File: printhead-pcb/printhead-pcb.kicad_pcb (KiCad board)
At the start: 2 copper layers, 35 x 35 mm, 4 parts, among them U3 EMC2302-2-AIZL-TR, U4 EMC2302-2-AIZL-TR, U5 ADS1015IDGS, U6 PCA9536D

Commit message: circuit finished?
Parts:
- removed U5: ADS1015IDGS, Package_SO:TSSOP-10_3x3mm_P0.5mm
- removed U6: PCA9536D, Package_SO:SOIC-8_3.9x4.9mm_P1.27mm
- added C10: 0.22µF, Capacitor_SMD:C_0402_1005Metric, F.Cu at (154.0, 74.5)
- added C11: 0.1µF, Capacitor_SMD:C_0402_1005Metric, F.Cu at (151.0, 81.5)
- added C4: 0.1µF, Capacitor_SMD:C_0402_1005Metric, F.Cu at (139.5, 55.5)
- added C5: 0.1µF, Capacitor_SMD:C_0402_1005Metric, F.Cu at (136.1, 60.5)
- added C6: 0.1µF, Capacitor_SMD:C_0402_1005Metric, F.Cu at (132.0, 62.0)
- added C7: 0.1µFC, Capacitor_SMD:C_0402_1005Metric, F.Cu at (141.5, 62.0)
- added C8: 0.1µF, Capacitor_SMD:C_0402_1005Metric, F.Cu at (136.1, 66.4)
- added C9: 1µF, Capacitor_SMD:C_0402_1005Metric, F.Cu at (149.8, 75.1)
- added D1: GREEN, LED_SMD:LED_0805_2012Metric, F.Cu at (154.5, 79.5)
- added D2: YELLOW, LED_SMD:LED_0805_2012Metric, F.Cu at (158.9, 66.5)
- added D3: BLUE, LED_SMD:LED_0805_2012Metric, F.Cu at (131.5, 77.5)
- added D4: YELLOW, LED_SMD:LED_0805_2012Metric, F.Cu at (155.5, 71.0)
- added J1: FAN0, Connector_JST:JST_GH_SM02B-GHS-TB_1x02-1MP_P1.25mm_Horizontal, F.Cu at (133.0, 52.0)
- added J2: FAN2, Connector_JST:JST_GH_SM02B-GHS-TB_1x02-1MP_P1.25mm_Horizontal, F.Cu at (110.5, 52.0)
- added J3: FAN1, Connector_JST:JST_GH_SM02B-GHS-TB_1x02-1MP_P1.25mm_Horizontal, F.Cu at (110.2, 66.4)
- added J4: FAN3, Connector_JST:JST_GH_SM02B-GHS-TB_1x02-1MP_P1.25mm_Horizontal, F.Cu at (110.2, 73.9)
- added J5: T0, Connector_JST:JST_GH_SM02B-GHS-TB_1x02-1MP_P1.25mm_Horizontal, F.Cu at (125.5, 52.0)
- added J6: T1, Connector_JST:JST_GH_SM02B-GHS-TB_1x02-1MP_P1.25mm_Horizontal, F.Cu at (110.2, 59.0)
- added J7: T2, Connector_JST:JST_GH_SM02B-GHS-TB_1x02-1MP_P1.25mm_Horizontal, F.Cu at (110.2, 81.5)
- added J8: T3, Connector_JST:JST_GH_SM02B-GHS-TB_1x02-1MP_P1.25mm_Horizontal, F.Cu at (118.0, 52.0)
- added L2: L, Inductor_SMD:L_0402_1005Metric, F.Cu at (134.5, 71.0)
- added L3: L, Inductor_SMD:L_0402_1005Metric, F.Cu at (129.5, 69.0)
- added L4: L, Inductor_SMD:L_0402_1005Metric, F.Cu at (131.0, 73.0)
- added L5: L, Inductor_SMD:L_0402_1005Metric, F.Cu at (139.0, 66.5)
- added L6: L, Inductor_SMD:L_0402_1005Metric, F.Cu at (146.9, 75.1)
- added Q1: DTC143E, Package_TO_SOT_SMD:SOT-723, F.Cu at (122.1, 60.4)
- added Q2: DTC143E, Package_TO_SOT_SMD:SOT-723, F.Cu at (125.0, 61.5)
- added Q3: DTC143E, Package_TO_SOT_SMD:SOT-723, F.Cu at (128.9, 60.0)
- added Q4: DTC143E, Package_TO_SOT_SMD:SOT-723, F.Cu at (120.9, 71.0)
- added R1: 10k, Resistor_SMD:R_0402_1005Metric, F.Cu at (144.5, 77.0)
- added R10: 10k, Resistor_SMD:R_0402_1005Metric, F.Cu at (126.0, 71.5)
- added R11: 330, Resistor_SMD:R_0402_1005Metric, F.Cu at (139.0, 69.5)
- added R12: 330, Resistor_SMD:R_0402_1005Metric, F.Cu at (146.0, 66.5)
- added R13: 330, Resistor_SMD:R_0402_1005Metric, F.Cu at (152.5, 66.5)
- added R14: 10k, Resistor_SMD:R_0402_1005Metric, F.Cu at (150.5, 70.0)
- added R15: 10k, Resistor_SMD:R_0402_1005Metric, F.Cu at (146.9, 71.1)
- added R17: 1k, Resistor_SMD:R_0402_1005Metric, F.Cu at (143.0, 81.5)
- added R2: 10k, Resistor_SMD:R_0402_1005Metric, F.Cu at (146.9, 81.5)
- added R20: 1k8, Resistor_SMD:R_0402_1005Metric, F.Cu at (132.5, 68.5)
- added R21: 1k8, Resistor_SMD:R_0402_1005Metric, F.Cu at (142.0, 65.5)
- added R25: 1k8, Resistor_SMD:R_0402_1005Metric, F.Cu at (142.0, 69.0)
- added R26: 1k8, Resistor_SMD:R_0402_1005Metric, F.Cu at (142.0, 72.4)
- added R3: 10k, Resistor_SMD:R_0402_1005Metric, F.Cu at (120.5, 57.0)
- added R4: 10k, Resistor_SMD:R_0402_1005Metric, F.Cu at (117.9, 60.5)
- added R5: 3k3, Resistor_SMD:R_0402_1005Metric, F.Cu at (116.5, 64.5)
- added R6: 3k3, Resistor_SMD:R_0402_1005Metric, F.Cu at (120.0, 66.5)
- added R7: 10k, Resistor_SMD:R_0402_1005Metric, F.Cu at (117.5, 69.5)
- added R8: 10k, Resistor_SMD:R_0402_1005Metric, F.Cu at (124.0, 67.8)
- added R9: 10k, Resistor_SMD:R_0402_1005Metric, F.Cu at (128.0, 66.0)
- added U1: EMC2302-1-AIZL-TR, EMC2302-1-AIZL-TR:MSOP10_MC_MCH-M, F.Cu at (120.6, 76.0)
- added U2: EMC2302-2-AIZL-TR, EMC2302-1-AIZL-TR:MSOP10_MC_MCH-M, F.Cu at (120.6, 81.2)
- U3: value EMC2302-2-AIZL-TR -> ADS1015IDGS; footprint EMC2302-2-AIZL-TR:MSOP10_MC_MCH-M -> Package_SO:TSSOP-10_3x3mm_P0.5mm
- U4: value EMC2302-2-AIZL-TR -> PCA9536D; footprint EMC2302-2-AIZL-TR:MSOP10_MC_MCH-M -> Package_SO:SOIC-8_3.9x4.9mm_P1.27mm
- moved U3 15.7 mm to (138.2, 75.7)
- moved U4 11.8 mm to (149.6, 60.9)
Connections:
- U3 pad 1: unconnected-(U3-SMDATA-Pad1) -> GND
- U3 pad 10: unconnected-(U3-*ALERT-Pad10) -> SCL
- U3 pad 2: unconnected-(U3-SMCLK-Pad2) -> Net-(D3-A)
- U3 pad 3: unconnected-(U3-VDD-Pad3) -> GND
- U3 pad 4: unconnected-(U3-GND-Pad4) -> ADC0
- U3 pad 5: unconnected-(U3-PWM1-Pad5) -> ADC1
- U3 pad 6: unconnected-(U3-TACH1-Pad6) -> ADC2
- U3 pad 7: unconnected-(U3-PWM2-Pad7) -> ADC3
- U3 pad 8: unconnected-(U3-TACH2-Pad8) -> +3.3V
- U3 pad 9: unconnected-(U3-CLK-Pad9) -> SDA
- U4 pad 1: unconnected-(U4-SMDATA-Pad1) -> IO0
- U4 pad 2: unconnected-(U4-SMCLK-Pad2) -> IO1
- U4 pad 3: unconnected-(U4-VDD-Pad3) -> IO2
- U4 pad 4: unconnected-(U4-GND-Pad4) -> GND
- U4 pad 5: unconnected-(U4-PWM1-Pad5) -> IO3
- U4 pad 6: unconnected-(U4-TACH1-Pad6) -> SDA
- U4 pad 7: unconnected-(U4-PWM2-Pad7) -> SDA
- U4 pad 8: unconnected-(U4-TACH2-Pad8) -> +3.3V
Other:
- board size 35 x 35 mm -> 55.5 x 37 mm
- board text added: "*"

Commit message: layout
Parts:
- removed L5, L6: L, Inductor_SMD:L_0402_1005Metric
- removed R21, R25, R26: 1k8, Resistor_SMD:R_0402_1005Metric
- added C1: 0.1µF, Capacitor_SMD:CP_Elec_5x3, B.Cu at (129.5, 60.0)
- added C2: 0.1µF, Capacitor_SMD:CP_Elec_5x3, F.Cu at (129.5, 60.0)
- added C3: 0.22µF, Capacitor_SMD:C_0402_1005Metric, B.Cu at (135.6, 75.0)
- added H1: MountingHole_Pad, MountingHole:MountingHole_2.2mm_M2_Pad_TopBottom, F.Cu at (140.5, 59.0)
- added H2: MountingHole_Pad, MountingHole:MountingHole_2.2mm_M2_Pad_TopBottom, F.Cu at (113.5, 80.0)
- added H3: MountingHole_Pad, MountingHole:MountingHole_2.2mm_M2_Pad_TopBottom, F.Cu at (113.5, 59.0)
- added H4: MountingHole_Pad, MountingHole:MountingHole_2.2mm_M2_Pad_TopBottom, F.Cu at (140.0, 80.0)
- added J1: PWR, Connector_JST:JST_EH_S5B-EH_1x05_P2.50mm_Horizontal, F.Cu at (128.0, 54.0)
- added J10: BL_TOUCH, Connector_JST:JST_EH_S2B-EH_1x02_P2.50mm_Horizontal, F.Cu at (108.5, 80.0)
- added L1: L, Inductor_SMD:L_0603_1608Metric, F.Cu at (134.7, 68.5)
- added R16: 4k7, Resistor_SMD:R_0402_1005Metric, F.Cu at (138.2, 76.2)
- added R18: 10k, Resistor_SMD:R_0402_1005Metric, F.Cu at (126.3, 74.3)
- added R19: 330, Resistor_SMD:R_0402_1005Metric, F.Cu at (126.3, 76.3)
- C10: value 0.22µF -> 0.1µFC
- C4: value 0.1µF -> 0.22µF; moved to B.Cu
- C5, C6, D1, Q1, Q2, Q3, Q4, R10, R2, R3, R4, R7, R8, R9: moved to B.Cu
- C7: value 0.1µFC -> 0.1µF
- C9: value 1µF -> 0.1µF
- D2: value YELLOW -> BLUE
- D3: value BLUE -> YELLOW
- J2: renamed from J1; footprint Connector_JST:JST_GH_SM02B-GHS-TB_1x02-1MP_P1.25mm_Horizontal -> Connector_JST:JST_EH_S2B-EH_1x02_P2.50mm_Horizontal
- J3: renamed from J2; footprint Connector_JST:JST_GH_SM02B-GHS-TB_1x02-1MP_P1.25mm_Horizontal -> Connector_JST:JST_EH_B2B-EH-A_1x02_P2.50mm_Vertical
- J4: renamed from J3; footprint Connector_JST:JST_GH_SM02B-GHS-TB_1x02-1MP_P1.25mm_Horizontal -> Connector_JST:JST_EH_S2B-EH_1x02_P2.50mm_Horizontal
- J5: renamed from J4; footprint Connector_JST:JST_GH_SM02B-GHS-TB_1x02-1MP_P1.25mm_Horizontal -> Connector_JST:JST_EH_B2B-EH-A_1x02_P2.50mm_Vertical
- J6: renamed from J5; footprint Connector_JST:JST_GH_SM02B-GHS-TB_1x02-1MP_P1.25mm_Horizontal -> Connector_JST:JST_EH_S2B-EH_1x02_P2.50mm_Horizontal
- J7: renamed from J6; footprint Connector_JST:JST_GH_SM02B-GHS-TB_1x02-1MP_P1.25mm_Horizontal -> Connector_JST:JST_EH_S2B-EH_1x02_P2.50mm_Horizontal
- J8: renamed from J7; footprint Connector_JST:JST_GH_SM02B-GHS-TB_1x02-1MP_P1.25mm_Horizontal -> Connector_JST:JST_EH_B2B-EH-A_1x02_P2.50mm_Vertical
- J9: renamed from J8; footprint Connector_JST:JST_GH_SM02B-GHS-TB_1x02-1MP_P1.25mm_Horizontal -> Connector_JST:JST_EH_B2B-EH-A_1x02_P2.50mm_Vertical
- L2, L3, L4: footprint Inductor_SMD:L_0402_1005Metric -> Inductor_SMD:L_0603_1608Metric
- R1: value 10k -> 1k; moved to B.Cu
- R11: value 330 -> 10k; moved to B.Cu
- R12, R13: value 330 -> 4k7
- R14: value 10k -> 330
- R15: value 10k -> 4k7
- R17: value 1k -> 10k
- R20: value 1k8 -> 330
- R5, R6: value 3k3 -> 10k; moved to B.Cu
- U1: value EMC2302-1-AIZL-TR -> EMC2302-2-AIZL-TR; footprint EMC2302-1-AIZL-TR:MSOP10_MC_MCH-M -> EMC2302-2-AIZL-TR:MSOP10_MC_MCH
- U2: footprint EMC2302-1-AIZL-TR:MSOP10_MC_MCH-M -> EMC2302-2-AIZL-TR:MSOP10_MC_MCH; moved to B.Cu
- moved D2 33.9 mm to (128.6, 81.5)
- moved J9 28.2 mm to (121.8, 80.0)
- moved D4 26.0 mm to (130.0, 75.9)
- moved D1 25.6 mm to (134.5, 63.5), turned to 180 degrees
- moved J2 23.3 mm to (109.8, 54.0), turned to 0 degrees
- moved U4 22.3 mm to (128.5, 68.0)
- moved R3 20.6 mm to (135.6, 71.1), turned to 180 degrees
- moved J6 19.7 mm to (108.5, 62.0), turned to 90 degrees
- moved R17 19.1 mm to (126.3, 72.4)
- moved C4 18.0 mm to (135.6, 73.0), turned to 180 degrees
- moved R2 16.8 mm to (135.6, 69.1), turned to 180 degrees
- moved U2 15.8 mm to (122.5, 65.5), turned to -90 degrees
- moved C6 15.4 mm to (135.6, 77.0), turned to 180 degrees
- moved J4 15.0 mm to (118.8, 54.0), turned to 0 degrees
- moved R13 14.8 mm to (138.2, 70.2)
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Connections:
- C10 pad 1: Net-(C10-Pad1) -> ADC2
- C11 pad 1: Net-(C10-Pad1) -> ADC3
- C4 pad 1: ADC0 -> +3V3
- C5 pad 1: +3.3V -> +12V
- C6 pad 1: ADC0 -> +3V3
- C8 pad 1: ADC0 -> +3.3V
- C9 pad 1: Net-(C10-Pad1) -> ADC1
- D2 pad 2: IO0 -> Net-(D2-A)
- D3 pad 2: Net-(D3-A) -> IO0
- L2 pad 1: TC0 -> TC1
- L2 pad 2: ADC0 -> ADC1
- L3 pad 1: TC0 -> TC2
- L3 pad 2: ADC0 -> ADC2
- L4 pad 1: TC0 -> TC3
- L4 pad 2: ADC0 -> ADC3
- R1 pad 1: +3V3 -> Net-(D1-K)
- R1 pad 2: SDA -> GND
- R10 pad 1: Net-(U2-CLK) -> Net-(U1-CLK)
- R11 pad 1: GND -> Net-(U2-CLK)
- R11 pad 2: Net-(D3-K) -> GND
- R12 pad 1: Net-(D2-K) -> AREF
- R12 pad 2: GND -> ADC0
- R13 pad 1: Net-(D4-K) -> AREF
- R13 pad 2: GND -> ADC1
- R14 pad 1: IO2 -> GND
- R14 pad 2: GND -> Net-(D2-K)
- R15 pad 1: IO3 -> AREF
- R15 pad 2: GND -> ADC2
- R17 pad 1: Net-(D1-K) -> IO3
- R2 pad 2: SCL -> SDA
- R20 pad 1: AREF -> Net-(D4-K)
- R20 pad 2: ADC0 -> GND
- R3 pad 1: Net-(U1-TACH1) -> +3V3
- R3 pad 2: GND -> SCL
- R4 pad 1: Net-(U2-TACH1) -> Net-(U1-TACH1)
- R5 pad 1: Net-(U1-*ALERT) -> Net-(U2-TACH1)
- R6 pad 1: Net-(U2-*ALERT) -> Net-(U1-*ALERT)
- R7 pad 1: Net-(U1-TACH2) -> Net-(U2-*ALERT)
- R8 pad 1: Net-(U2-TACH2) -> Net-(U1-TACH2)
- R9 pad 1: Net-(U1-CLK) -> Net-(U2-TACH2)
- U3 pad 2: Net-(D3-A) -> Net-(D2-A)
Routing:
- added copper zone on B.Cu, net GND
- added copper zone on F.Cu, net GND
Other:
- board size 55.5 x 37 mm -> 37 x 35 mm
- board text removed: "*"

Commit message: first pcb layout
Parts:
- C6, D1, R1, R2, R3: moved to F.Cu
- C7, C9, L2, R12, R13, U1, U3: moved to B.Cu
- moved L1 22.5 mm to (113.0, 62.5)
- moved L2 20.3 mm to (115.0, 76.0)
- moved R11 18.8 mm to (127.5, 76.0), turned to 0 degrees
- moved C8 16.5 mm to (126.0, 63.5)
- moved C11 15.6 mm to (126.0, 80.0), turned to -90 degrees
- moved C10 15.4 mm to (126.0, 71.0), turned to 180 degrees
- moved C6 15.4 mm to (126.0, 65.0), turned to 0 degrees
- moved R19 14.3 mm to (133.5, 64.0), turned to 90 degrees
- moved R17 13.3 mm to (139.5, 73.5)
- moved C3 13.0 mm to (129.5, 63.5)
- moved L3 12.2 mm to (122.5, 74.0)
- moved L4 12.2 mm to (122.5, 76.0)
- moved C5 11.7 mm to (129.5, 64.5)
- moved R15 11.7 mm to (126.5, 74.0), turned to 180 degrees
- moved R16 11.7 mm to (126.5, 76.0), turned to 180 degrees
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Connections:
- C8 pad 1: +3.3V -> +3V3
- J10 pad 1: GND -> IO2
- J10 pad 2: IO2 -> +3V3
- U3 pad 8: +3.3V -> +3V3
- U4 pad 6: SDA -> SCL
- U4 pad 8: +3.3V -> +3V3
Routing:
- net GND: track 0.00 -> 265.1 mm, vias 0 -> 4
- net +3V3: track 0.00 -> 76.0 mm, vias 0 -> 6
- net SCL: track 0.00 -> 65.9 mm, vias 0 -> 1
- net +12V: track 0.00 -> 53.1 mm, vias 0 -> 1
- net SDA: track 0.00 -> 52.7 mm, vias 0 -> 1
- net IO2: track 0.00 -> 32.6 mm
- net ADC0: track 0.00 -> 31.1 mm, vias 0 -> 1
- net ADC1: track 0.00 -> 28.9 mm
- net AREF: track 0.00 -> 28.8 mm, vias 0 -> 1
- net Net-(J3-Pin_1): track 0.00 -> 18.2 mm, vias 0 -> 1
- net ADC3: track 0.00 -> 17.5 mm, vias 0 -> 1
- net Net-(J2-Pin_1): track 0.00 -> 15.6 mm
- net ADC2: track 0.00 -> 14.7 mm, vias 0 -> 1
- net Net-(J4-Pin_1): track 0.00 -> 13.0 mm
- net Net-(D2-A): track 0.00 -> 10.9 mm, vias 0 -> 1
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
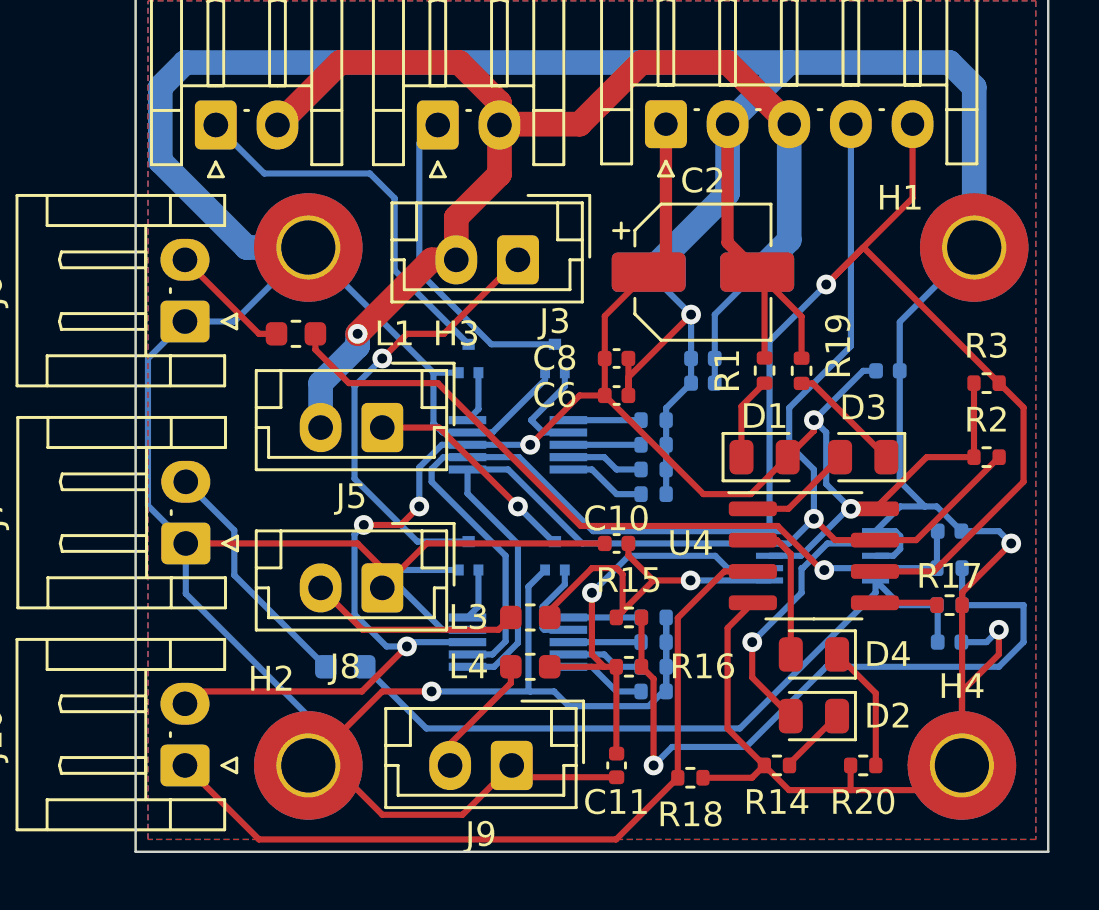
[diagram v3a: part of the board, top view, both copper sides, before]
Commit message: rename datasheets
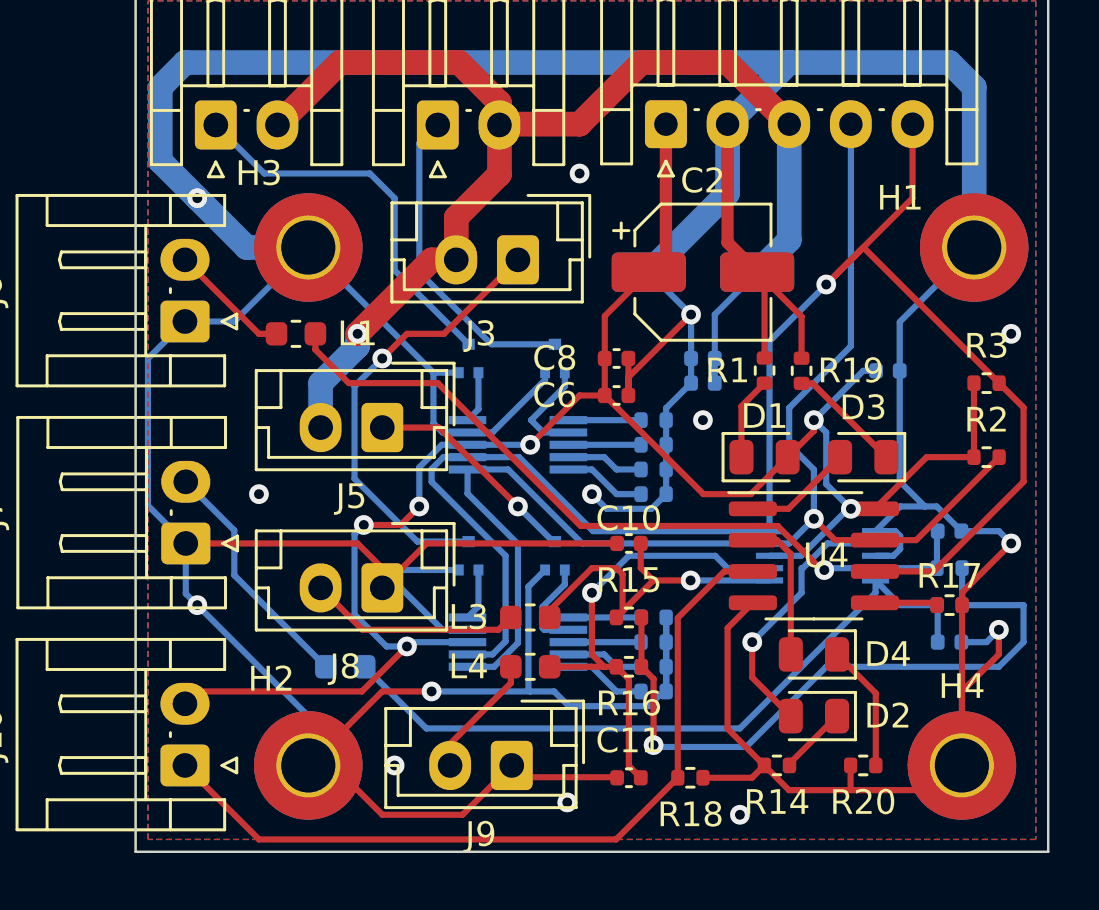
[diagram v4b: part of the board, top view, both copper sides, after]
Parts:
- moved C11 0.71 mm to (126.5, 80.5), turned to 180 degrees
- moved C10 0.50 mm to (126.5, 71.0)
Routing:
- net GND: track 265.1 -> 269.1 mm, vias 4 -> 14
- net ADC3: track 17.5 -> 18.8 mm
- net AREF: track 28.8 -> 27.7 mm

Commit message: smaller layout
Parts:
- moved R2 3.91 mm to (138.0, 65.0)
- moved R3 3.16 mm to (138.0, 63.5)
- moved H1 2.50 mm to (138.0, 59.0)
- moved R14 2.12 mm to (134.0, 81.5)
- moved H4 2.00 mm to (138.0, 80.0)
- moved R20 2.00 mm to (134.0, 80.0)
- moved C7 0.50 mm to (139.0, 70.5)
- moved C9 0.50 mm to (139.0, 75.0)
- moved R12 0.50 mm to (139.0, 72.0)
- moved R13 0.50 mm to (139.0, 73.5)
- moved R17 0.50 mm to (139.0, 73.5)
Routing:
- net GND: track 269.1 -> 250.6 mm, vias 14 -> 11
- net SCL: track 65.9 -> 62.3 mm
- net AREF: track 27.7 -> 24.3 mm
- net SDA: track 52.7 -> 54.4 mm
- net Net-(D2-K): track 2.80 -> 4.08 mm
- net IO3: track 2.55 -> 2.05 mm
- net ADC1: track 28.9 -> 28.4 mm
- net ADC0: track 31.1 -> 30.6 mm
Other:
- board size 37 x 35 mm -> 35 x 35 mm
